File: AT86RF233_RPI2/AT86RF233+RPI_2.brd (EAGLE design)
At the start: 23.6 x 43.1 mm, 10 parts, among them SW1 KSR2XYG, U1 ATZB-RF-233-1-C

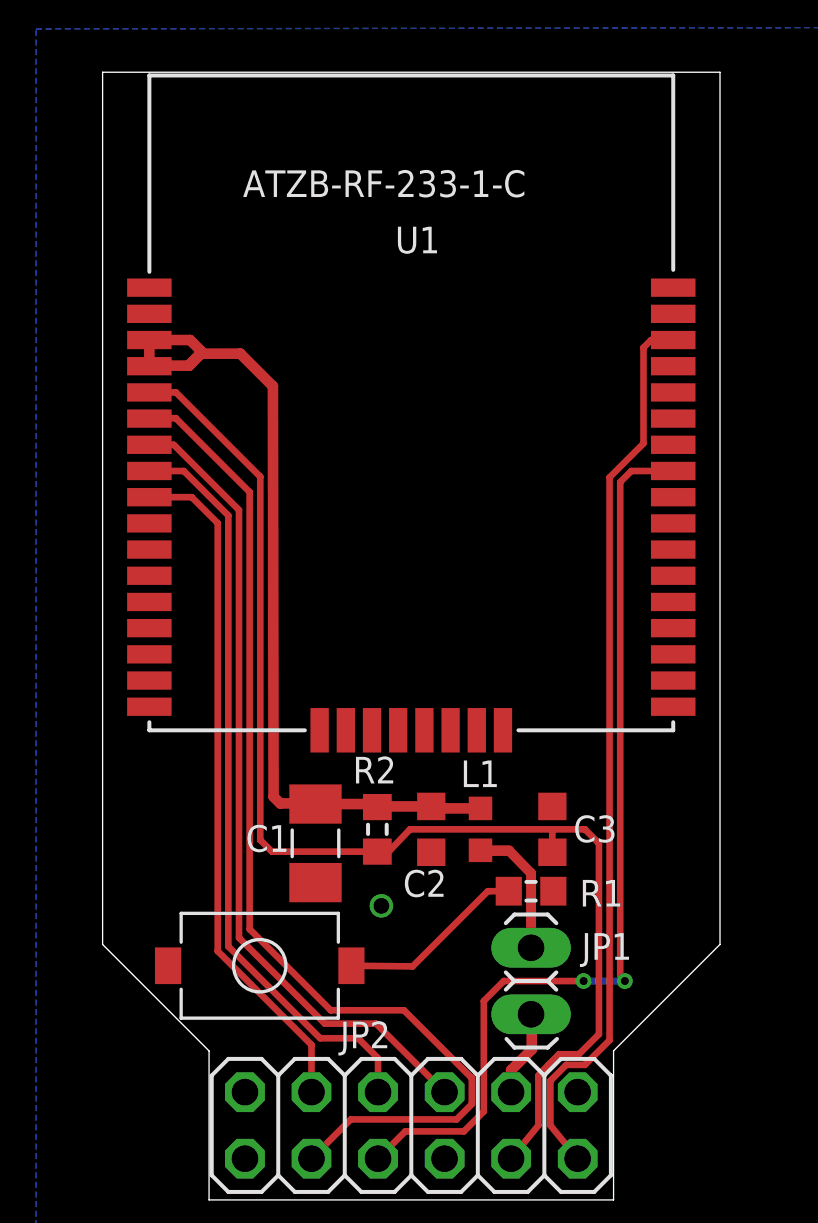
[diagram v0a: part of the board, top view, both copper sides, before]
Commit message: at86rf233: SW1 renamed to RESET & minor alignemt improvements.
Signed-off-by: malo <malo@25cmsquare.io>
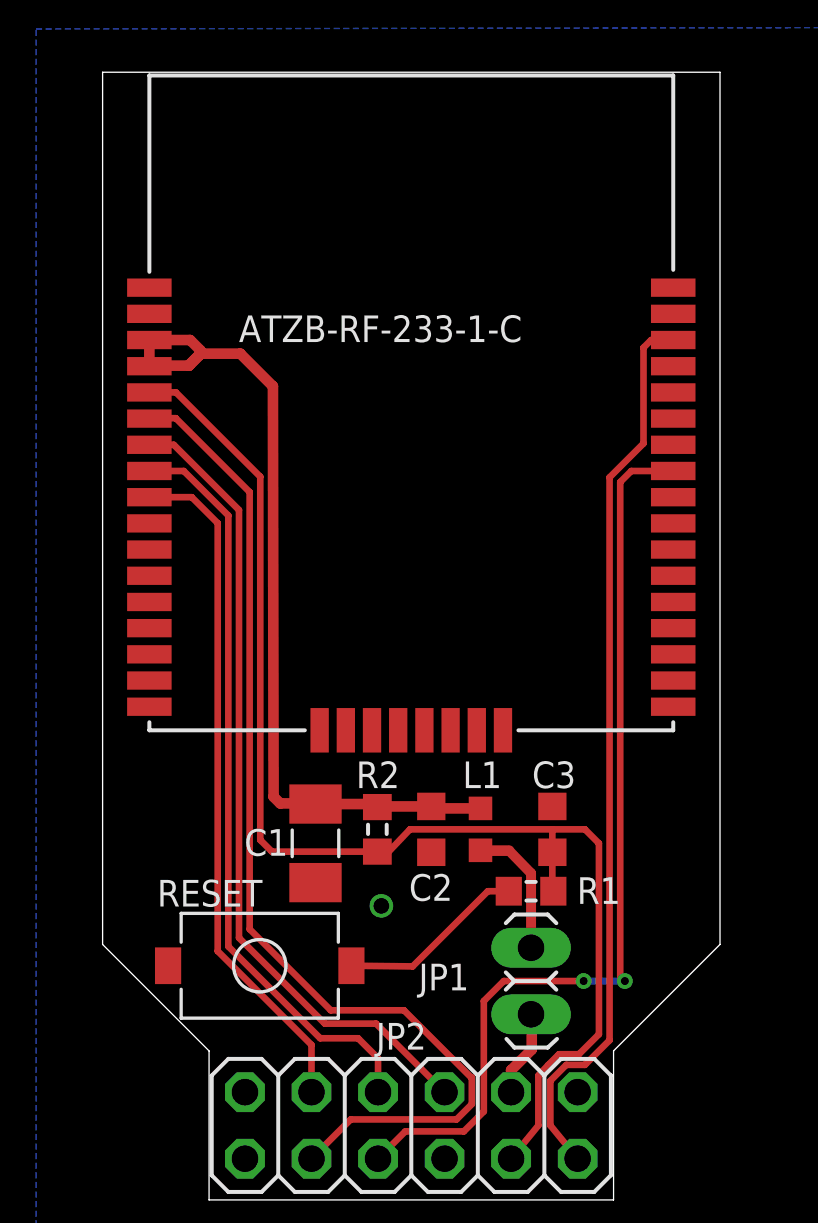
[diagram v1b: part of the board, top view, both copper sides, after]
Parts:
- renumbered SW1 to RESET
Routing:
- net NRESET: track 48.2 -> 49.7 mm
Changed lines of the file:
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@@
 <element name="C1" library="resistor" package="C1206K" value="TANTAL 10u 16V 1206, TR3A106K016C" x="8.128" y="13.6144" smashed="yes" rot="R270">
 <attribute name="SPICEPREFIX" value="C" x="8.128" y="13.6144" size="1.778" layer="27" rot="R270" display="off"/>
-<attribute name="NAME" x="5.461196875" y="13.292" size="1.016" layer="25" font="vector" ratio="15"/>
+<attribute name="NAME" x="5.410396875" y="13.1396" size="1.016" layer="25" font="vector" ratio="15"/>
 </element>
 <element name="C2" library="rcl" package="C0603K" value="1nF, 0603, GRM155R71H1 02K" x="12.5476" y="14.1478" smashed="yes" rot="R270">
-<attribute name="NAME" x="11.4682" y="11.572" size="1.016" layer="25" font="vector" ratio="15"/>
+<attribute name="NAME" x="11.6968" y="11.4196" size="1.016" layer="25" font="vector" ratio="15"/>
 </element>
 <element name="C3" library="rcl" package="C0603K" value="4n7, 0603" x="17.1704" y="14.1478" smashed="yes" rot="R90">
-<attribute name="NAME" x="17.9706" y="13.6548" size="1.016" layer="25" font="vector" ratio="15"/>
+<attribute name="NAME" x="16.3958" y="15.7226" size="1.016" layer="25" font="vector" ratio="15"/>
 </element>
 <element name="JP1" library="pinhead" package="1X02" value="" x="16.3576" y="8.3566" smashed="yes" rot="R90">
-<attribute name="NAME" x="18.288" y="9.1694" size="1.016" layer="25" font="vector" ratio="15"/>
+<attribute name="NAME" x="12.065" y="8.001" size="1.016" layer="25" font="vector" ratio="15"/>
 <attribute name="VALUE" x="19.5326" y="5.8166" size="1.27" layer="27" rot="R90"/>
 </element>
 <element name="JP2" library="pinhead" package="2X06" value="" x="11.7856" y="2.8448" smashed="yes" rot="R180">
-<attribute name="NAME" x="9.0678" y="5.7912" size="1.016" layer="25" font="vector" ratio="15"/>
+<attribute name="NAME" x="10.4394" y="5.7404" size="1.016" layer="25" font="vector" ratio="15"/>
 <attribute name="VALUE" x="19.4056" y="7.2898" size="1.27" layer="27" rot="R180"/>
 </element>
 <element name="L1" library="25cmsquare" package="L0603" value="BLM18PG471SN1" x="14.4272" y="14.1478" smashed="yes" rot="R90">
-<attribute name="NAME" x="13.6694" y="15.7614" size="1.016" layer="25" font="vector" ratio="15"/>
+<attribute name="NAME" x="13.7456" y="15.7226" size="1.016" layer="25" font="vector" ratio="15"/>
 </element>
 <element name="R1" library="resistor" package="R0603" value="39R, 0603" x="16.3576" y="11.7856" smashed="yes">
 <attribute name="SPICEPREFIX" value="R" x="16.3576" y="11.7856" size="1.778" layer="27" display="off"/>
-<attribute name="NAME" x="18.2118" y="11.2014" size="1.016" layer="25" font="vector" ratio="15"/>
+<attribute name="NAME" x="18.1102" y="11.303" size="1.016" layer="25" font="vector" ratio="15"/>
 </element>
 <element name="R2" library="resistor" package="R0603" value="100k, 0603" x="10.4902" y="14.1478" smashed="yes" rot="R90">
 <attribute name="SPICEPREFIX" value="R" x="10.4902" y="14.1478" size="1.778" layer="27" rot="R90" display="off"/>
-<attribute name="NAME" x="9.5504" y="15.9004" size="1.016" layer="25" font="vector" ratio="15"/>
-</element>
-<element name="SW1" library="25cmsquare" package="KSR2XYG" value="KSR2XYG" x="9.4996" y="8.9408" smashed="yes" rot="R90"/>
+<attribute name="NAME" x="9.6774" y="15.7226" size="1.016" layer="25" font="vector" ratio="15"/>
+</element>
+<element name="RESET" library="25cmsquare" package="KSR2XYG" value="KSR2XYG" x="9.4996" y="8.9408" smashed="yes" rot="R90">
+<attribute name="NAME" x="2.0828" y="11.2014" size="1.016" layer="21" font="vector" ratio="15"/>
+</element>
 <element name="U1" library="25cmsquare" package="ATZB-RF-233-1-C" value="ATZB-RF-233-1-C" x="11.7856" y="30.4292" smashed="yes" rot="R180">
-<attribute name="NAME" x="12.8816" y="37.1556" size="1.016" layer="21" font="vector" ratio="15" rot="R180"/>
-<attribute name="VALUE" x="5.3556" y="38.2892" size="1.016" layer="21" font="vector" ratio="15"/>
+<attribute name="VALUE" x="5.2032" y="32.752" size="1.016" layer="21" font="vector" ratio="15"/>
 </element>
 </elements>
@@
 <contactref element="JP2" pad="11"/>
 <contactref element="JP2" pad="6"/>
-<contactref element="SW1" pad="P$2"/>
+<contactref element="RESET" pad="P$2"/>
 <contactref element="C3" pad="2"/>
 <polygon width="0.4064" layer="16">
@@
 <wire x1="18.415" y1="14.1478" x2="18.9484" y2="13.6144" width="0.254" layer="1"/>
 <wire x1="17.1704" y1="13.2728" x2="17.1704" y2="14.1478" width="0.254" layer="1"/>
-<wire x1="17.1704" y1="13.2728" x2="17.2076" y2="11.7856" width="0" layer="19" extent="1-1"/>
+<wire x1="17.2076" y1="11.7856" x2="17.1704" y2="11.7856" width="0.254" layer="1"/>
+<wire x1="17.1704" y1="11.7856" x2="17.1704" y2="13.2728" width="0.254" layer="1"/>
 </signal>
 <signal name="SLP_TR">
@@
 <signal name="N$1">
 <contactref element="R1" pad="1"/>
-<contactref element="SW1" pad="P$1"/>
+<contactref element="RESET" pad="P$1"/>
 <wire x1="9.4996" y1="8.9408" x2="11.8364" y2="8.9154" width="0.254" layer="1"/>
 <wire x1="11.8364" y1="8.9154" x2="14.7066" y2="11.7856" width="0.254" layer="1"/>
